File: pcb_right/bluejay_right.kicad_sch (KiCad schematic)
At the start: 60 parts, among them J2 SJ-43514, SW2B KEYSW, SW2C KEYSW, SW2D KEYSW, SW2E KEYSW, SW2F KEYSW, SW3A KEYSW, SW3B KEYSW, SW3C KEYSW, SW3D KEYSW, SW3E KEYSW, SW3F KEYSW, SW4A KEYSW, SW4B KEYSW, SW4C KEYSW, SW4D KEYSW, SW4E KEYSW, SW4F KEYSW, SW5A KEYSW, SW5B KEYSW, SW5C KEYSW, SW5D KEYSW, U2 MCP23017

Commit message: Some updates to schematics before moving to pcb design
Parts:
- C6: footprint (none) -> BlueJay footprints:CP_Radial_D4.0mm_P1.50mm
- C7: footprint (none) -> BlueJay footprints:C_Disc_D4.3mm_W1.9mm_P5.00mm
- J2: footprint CUI_SJ-43514 -> BlueJay footprints:CUI_SJ-43514
- R5, R6: footprint (none) -> BlueJay footprints:R_Axial_DIN0204_L3.6mm_D1.6mm_P5.08mm_Horizontal
- SWa1, SWa2, SWb1, SWc1, SWd1, SWe1: footprint (none) -> BlueJay footprints:Kailh_socket_MX
- SWa3: renamed from SW3A; footprint (none) -> BlueJay footprints:Kailh_socket_MX
- SWa4: renamed from SW4A; footprint (none) -> BlueJay footprints:Kailh_socket_MX
- SWa5: renamed from SW5A; footprint (none) -> BlueJay footprints:Kailh_socket_MX
- SWb2: renamed from SW2B; footprint (none) -> BlueJay footprints:Kailh_socket_MX
- SWb3: renamed from SW3B; footprint (none) -> BlueJay footprints:Kailh_socket_MX
- SWb4: renamed from SW4B; footprint (none) -> BlueJay footprints:Kailh_socket_MX
- SWb5: renamed from SW5B; footprint (none) -> BlueJay footprints:Kailh_socket_MX
- SWc2: renamed from SW2C; footprint (none) -> BlueJay footprints:Kailh_socket_MX
- SWc3: renamed from SW3C; footprint (none) -> BlueJay footprints:Kailh_socket_MX
- SWc4: renamed from SW4C; footprint (none) -> BlueJay footprints:Kailh_socket_MX
- SWc5: renamed from SW5C; footprint (none) -> BlueJay footprints:Kailh_socket_MX
- SWd2: renamed from SW2D; footprint (none) -> BlueJay footprints:Kailh_socket_MX
- SWd3: renamed from SW3D; footprint (none) -> BlueJay footprints:Kailh_socket_MX
- SWd4: renamed from SW4D; footprint (none) -> BlueJay footprints:Kailh_socket_MX
- SWd5: renamed from SW5D; footprint (none) -> BlueJay footprints:Kailh_socket_MX
- SWe2: renamed from SW2E; footprint (none) -> BlueJay footprints:Kailh_socket_MX
- SWe3: renamed from SW3E; footprint (none) -> BlueJay footprints:Kailh_socket_MX
- SWe4: renamed from SW4E; footprint (none) -> BlueJay footprints:Kailh_socket_MX
- SWf2: renamed from SW2F; footprint (none) -> BlueJay footprints:Kailh_socket_MX
- SWf3: renamed from SW3F; footprint (none) -> BlueJay footprints:Kailh_socket_MX
- SWf4: renamed from SW4F; footprint (none) -> BlueJay footprints:Kailh_socket_MX
- renumbered D3A to Da3, D4A to Da4, D5A to Da5, D2B to Db2, D3B to Db3, D4B to Db4, D5B to Db5, D2C to Dc2, D3C to Dc3, D4C to Dc4, D5C to Dc5, D2D to Dd2, D3D to Dd3, D4D to Dd4, D5D to Dd5, D2E to De2, D3E to De3, D4E to De4, D2F to Df2, D3F to Df3, D4F to Df4

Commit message: Work on PCBs
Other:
- title: (none) -> BlueJay Right
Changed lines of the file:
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@@
 (kicad_sch (version 20211123) (generator eeschema)
   (paper "USLetter")
+  (title_block
+    (title "BlueJay Right")
+  )
   (junction (at 194.31 62.23) (diameter 0) (color 0 0 0 0)
   )

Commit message: Begin work on right pcb
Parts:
- Da1, Da2, Da3, Da4, Da5, Db1, Db2, Db3, Db4, Db5, Dc1, Dc2, Dc3, Dc4, Dc5, Dd1, Dd2, Dd3, Dd4, Dd5, De1, De2, De3, De4, Df2, Df3, Df4: footprint Diode_THT_AKL:D_DO-35_SOD27_P7.62mm_Horizontal -> BlueJay footprints:D_DO-35_SOD27_P5.08mm_Horizontal
- SWa1, SWa2, SWa3, SWa4, SWa5, SWb1, SWb2, SWb3, SWb4, SWb5, SWc1, SWc2, SWc3, SWc4, SWc5, SWd1, SWd2, SWd3, SWd4, SWd5, SWe1, SWe2, SWe3, SWe4, SWf2, SWf3, SWf4: footprint BlueJay footprints:Kailh_socket_MX -> BlueJay footprints:SW_MX

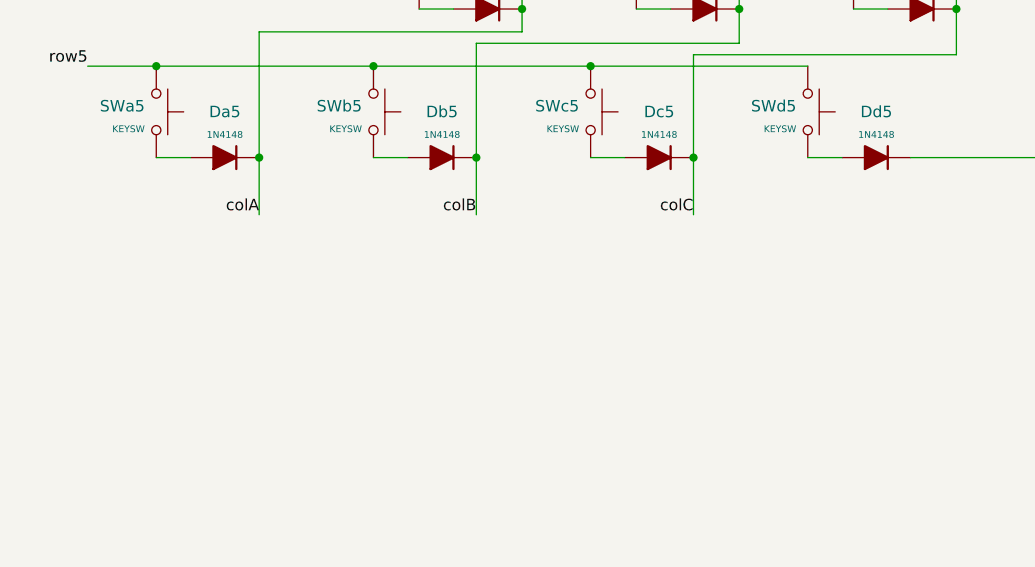
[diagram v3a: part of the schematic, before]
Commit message: Add mounting holes
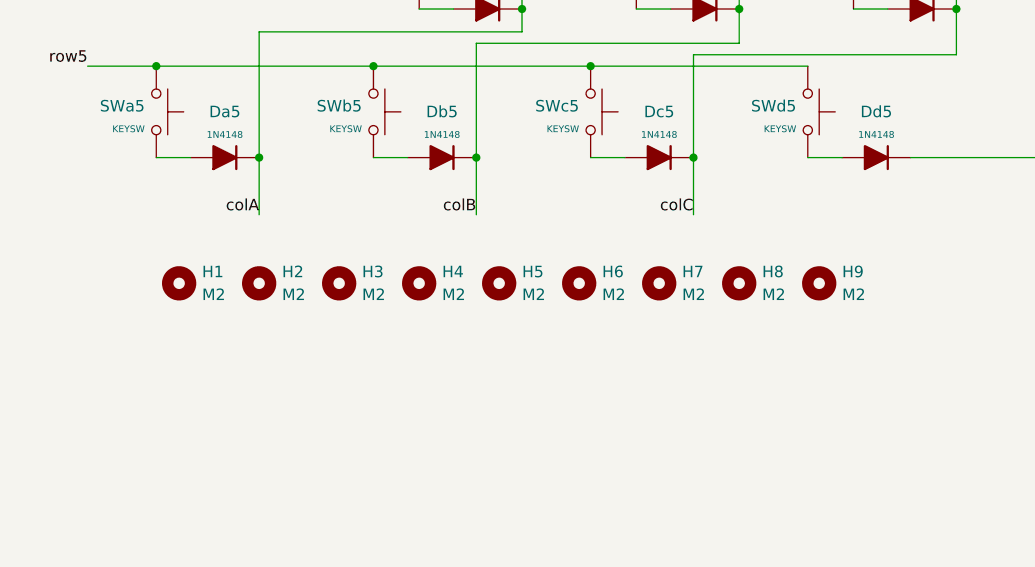
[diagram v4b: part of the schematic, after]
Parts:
- added H1, H2, H3, H4, H5, H6, H7, H8, H9: M2, MountingHole:MountingHole_2.2mm_M2_Pad, symbol Mechanical:MountingHole
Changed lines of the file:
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@@
     (pin "2")
+  )
+  (symbol (lib_id "Mechanical:MountingHole") (at 148.59 115.57 0) (unit 1)
+    (in_bom no) (on_board yes) (fields_autoplaced)
+    (property "Reference" "H7" (id 0) (at 151.13 114.2999 0)
+      (effects (font (size 1.27 1.27)) (justify left))
+    )
+    (property "Value" "M2" (id 1) (at 151.13 116.8399 0)
+      (effects (font (size 1.27 1.27)) (justify left))
+    )
+    (property "Footprint" "MountingHole:MountingHole_2.2mm_M2_Pad" (id 2) (at 148.59 115.57 0)
+      (effects (font (size 1.27 1.27)) hide)
+    )
+    (property "Datasheet" "~" (id 3) (at 148.59 115.57 0)
+      (effects (font (size 1.27 1.27)) hide)
+    )
   )
   (symbol (lib_id "BlueJaySymbolLibrary:Interface_Expansion_MCP23017_SP") (at 45.72 109.22 0) (unit 1)
@@
     (pin "9")
   )
+  (symbol (lib_id "Mechanical:MountingHole") (at 113.03 115.57 0) (unit 1)
+    (in_bom no) (on_board yes) (fields_autoplaced)
+    (property "Reference" "H3" (id 0) (at 115.57 114.2999 0)
+      (effects (font (size 1.27 1.27)) (justify left))
+    )
+    (property "Value" "M2" (id 1) (at 115.57 116.8399 0)
+      (effects (font (size 1.27 1.27)) (justify left))
+    )
+    (property "Footprint" "MountingHole:MountingHole_2.2mm_M2_Pad" (id 2) (at 113.03 115.57 0)
+      (effects (font (size 1.27 1.27)) hide)
+    )
+    (property "Datasheet" "~" (id 3) (at 113.03 115.57 0)
+      (effects (font (size 1.27 1.27)) hide)
+    )
+  )
   (symbol (lib_id "Diode_AKL:1N4148") (at 201.93 46.99 0) (mirror x) (unit 1)
     (in_bom yes) (on_board yes) (fields_autoplaced)
@@
     (pin "2")
   )
+  (symbol (lib_id "Mechanical:MountingHole") (at 104.14 115.57 0) (unit 1)
+    (in_bom no) (on_board yes) (fields_autoplaced)
+    (property "Reference" "H2" (id 0) (at 106.68 114.2999 0)
+      (effects (font (size 1.27 1.27)) (justify left))
+    )
+    (property "Value" "M2" (id 1) (at 106.68 116.8399 0)
+      (effects (font (size 1.27 1.27)) (justify left))
+    )
+    (property "Footprint" "MountingHole:MountingHole_2.2mm_M2_Pad" (id 2) (at 104.14 115.57 0)
+      (effects (font (size 1.27 1.27)) hide)
+    )
+    (property "Datasheet" "~" (id 3) (at 104.14 115.57 0)
+      (effects (font (size 1.27 1.27)) hide)
+    )
+  )
   (symbol (lib_id "power:GND") (at 45.72 139.7 0) (unit 1)
     (in_bom yes) (on_board yes) (fields_autoplaced)
@@
     )
     (pin "1")
+  )
+  (symbol (lib_id "Mechanical:MountingHole") (at 166.37 115.57 0) (unit 1)
+    (in_bom no) (on_board yes) (fields_autoplaced)
+    (property "Reference" "H9" (id 0) (at 168.91 114.2999 0)
+      (effects (font (size 1.27 1.27)) (justify left))
+    )
+    (property "Value" "M2" (id 1) (at 168.91 116.8399 0)
+      (effects (font (size 1.27 1.27)) (justify left))
+    )
+    (property "Footprint" "MountingHole:MountingHole_2.2mm_M2_Pad" (id 2) (at 166.37 115.57 0)
+      (effects (font (size 1.27 1.27)) hide)
+    )
+    (property "Datasheet" "~" (id 3) (at 166.37 115.57 0)
+      (effects (font (size 1.27 1.27)) hide)
+    )
   )
   (symbol (lib_id "BlueJaySymbolLibrary:Switch_SW_Push") (at 194.31 54.61 270) (mirror x) (unit 1)
@@
     (pin "2")
   )
+  (symbol (lib_id "Mechanical:MountingHole") (at 130.81 115.57 0) (unit 1)
+    (in_bom no) (on_board yes) (fields_autoplaced)
+    (property "Reference" "H5" (id 0) (at 133.35 114.2999 0)
+      (effects (font (size 1.27 1.27)) (justify left))
+    )
+    (property "Value" "M2" (id 1) (at 133.35 116.8399 0)
+      (effects (font (size 1.27 1.27)) (justify left))
+    )
+    (property "Footprint" "MountingHole:MountingHole_2.2mm_M2_Pad" (id 2) (at 130.81 115.57 0)
+      (effects (font (size 1.27 1.27)) hide)
+    )
+    (property "Datasheet" "~" (id 3) (at 130.81 115.57 0)
+      (effects (font (size 1.27 1.27)) hide)
+    )
+  )
   (symbol (lib_id "BlueJaySymbolLibrary:Device_R_Small") (at 55.88 46.99 0) (unit 1)
     (in_bom yes) (on_board yes) (fields_autoplaced)
@@
     (pin "1")
     (pin "2")
+  )
+  (symbol (lib_id "Mechanical:MountingHole") (at 139.7 115.57 0) (unit 1)
+    (in_bom no) (on_board yes) (fields_autoplaced)
+    (property "Reference" "H6" (id 0) (at 142.24 114.2999 0)
+      (effects (font (size 1.27 1.27)) (justify left))
+    )
+    (property "Value" "M2" (id 1) (at 142.24 116.8399 0)
+      (effects (font (size 1.27 1.27)) (justify left))
+    )
+    (property "Footprint" "MountingHole:MountingHole_2.2mm_M2_Pad" (id 2) (at 139.7 115.57 0)
+      (effects (font (size 1.27 1.27)) hide)
+    )
+    (property "Datasheet" "~" (id 3) (at 139.7 115.57 0)
+      (effects (font (size 1.27 1.27)) hide)
+    )
   )
   (symbol (lib_id "Diode_AKL:1N4148") (at 153.67 46.99 0) (mirror x) (unit 1)
@@
     (pin "1")
   )
+  (symbol (lib_id "Mechanical:MountingHole") (at 121.92 115.57 0) (unit 1)
+    (in_bom no) (on_board yes) (fields_autoplaced)
+    (property "Reference" "H4" (id 0) (at 124.46 114.2999 0)
+      (effects (font (size 1.27 1.27)) (justify left))
+    )
+    (property "Value" "M2" (id 1) (at 124.46 116.8399 0)
+      (effects (font (size 1.27 1.27)) (justify left))
+    )
+    (property "Footprint" "MountingHole:MountingHole_2.2mm_M2_Pad" (id 2) (at 121.92 115.57 0)
+      (effects (font (size 1.27 1.27)) hide)
+    )
+    (property "Datasheet" "~" (id 3) (at 121.92 115.57 0)
+      (effects (font (size 1.27 1.27)) hide)
+    )
+  )
   (symbol (lib_id "BlueJaySymbolLibrary:Switch_SW_Push") (at 121.92 67.31 270) (mirror x) (unit 1)
     (in_bom yes) (on_board yes) (fields_autoplaced)
@@
     (pin "1")
     (pin "2")
+  )
+  (symbol (lib_id "Mechanical:MountingHole") (at 95.25 115.57 0) (unit 1)
+    (in_bom no) (on_board yes) (fields_autoplaced)
+    (property "Reference" "H1" (id 0) (at 97.79 114.2999 0)
+      (effects (font (size 1.27 1.27)) (justify left))
+    )
+    (property "Value" "M2" (id 1) (at 97.79 116.8399 0)
+      (effects (font (size 1.27 1.27)) (justify left))
+    )
+    (property "Footprint" "MountingHole:MountingHole_2.2mm_M2_Pad" (id 2) (at 95.25 115.57 0)
+      (effects (font (size 1.27 1.27)) hide)
+    )
+    (property "Datasheet" "~" (id 3) (at 95.25 115.57 0)
+      (effects (font (size 1.27 1.27)) hide)
+    )
   )
   (symbol (lib_id "BlueJaySymbolLibrary:Switch_SW_Push") (at 146.05 80.01 270) (mirror x) (unit 1)
@@
     (pin "1")
   )
+  (symbol (lib_id "Mechanical:MountingHole") (at 157.48 115.57 0) (unit 1)
+    (in_bom no) (on_board yes) (fields_autoplaced)
+    (property "Reference" "H8" (id 0) (at 160.02 114.2999 0)
+      (effects (font (size 1.27 1.27)) (justify left))
+    )
+    (property "Value" "M2" (id 1) (at 160.02 116.8399 0)
+      (effects (font (size 1.27 1.27)) (justify left))
+    )
+    (property "Footprint" "MountingHole:MountingHole_2.2mm_M2_Pad" (id 2) (at 157.48 115.57 0)
+      (effects (font (size 1.27 1.27)) hide)
+    )
+    (property "Datasheet" "~" (id 3) (at 157.48 115.57 0)
+      (effects (font (size 1.27 1.27)) hide)
+    )
+  )
   (symbol (lib_id "Diode_AKL:1N4148") (at 153.67 72.39 0) (mirror x) (unit 1)
     (in_bom yes) (on_board yes) (fields_autoplaced)
@@
       (reference "Df4") (unit 1) (value "1N4148") (footprint "BlueJay footprints:D_DO-35_SOD27_P5.08mm_Horizontal")
     )
+    (path "/e3a864c6-2e05-4a63-b022-da7d340645e3"
+      (reference "H1") (unit 1) (value "M2") (footprint "MountingHole:MountingHole_2.2mm_M2_Pad")
+    )
+    (path "/29cea050-3e29-419d-ad47-3e79a1eb9101"
+      (reference "H2") (unit 1) (value "M2") (footprint "MountingHole:MountingHole_2.2mm_M2_Pad")
+    )
+    (path "/17614258-4f06-4822-913f-021afed04082"
+      (reference "H3") (unit 1) (value "M2") (footprint "MountingHole:MountingHole_2.2mm_M2_Pad")
+    )
+    (path "/e175d568-d75e-4a79-8707-a3c7001d62d8"
+      (reference "H4") (unit 1) (value "M2") (footprint "MountingHole:MountingHole_2.2mm_M2_Pad")
+    )
+    (path "/6076ed14-f492-4b0a-917b-dfd270a3bad8"
+      (reference "H5") (unit 1) (value "M2") (footprint "MountingHole:MountingHole_2.2mm_M2_Pad")
+    )
+    (path "/898f562a-635b-4ca8-9b29-632b29153076"
+      (reference "H6") (unit 1) (value "M2") (footprint "MountingHole:MountingHole_2.2mm_M2_Pad")
+    )
+    (path "/122e03f9-b490-4614-ab57-8a45c16d7cab"
+      (reference "H7") (unit 1) (value "M2") (footprint "MountingHole:MountingHole_2.2mm_M2_Pad")
+    )
+    (path "/ef6bf8a6-53c5-40a0-b55f-f0f6022fe6b3"
+      (reference "H8") (unit 1) (value "M2") (footprint "MountingHole:MountingHole_2.2mm_M2_Pad")
+    )
+    (path "/2f72a678-d445-4b98-b401-be2796bd34c3"
+      (reference "H9") (unit 1) (value "M2") (footprint "MountingHole:MountingHole_2.2mm_M2_Pad")
+    )
     (path "/36a90cbb-ec70-4202-aacd-9cf629bac560"

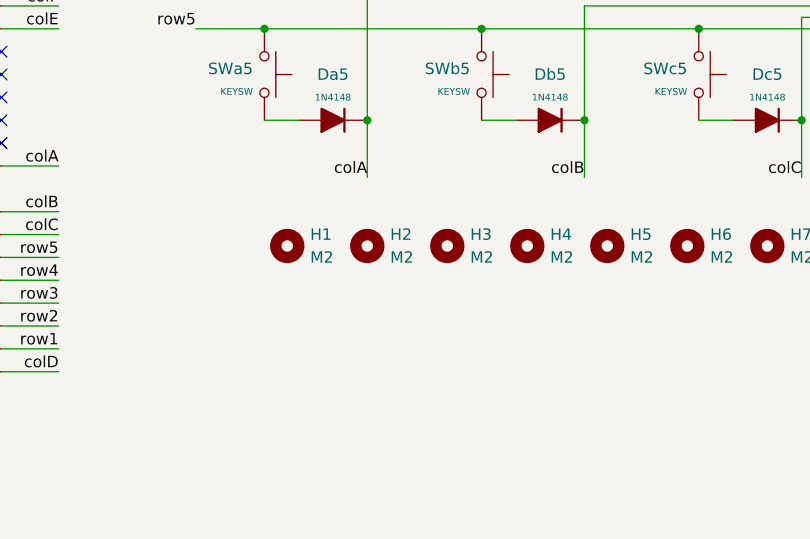
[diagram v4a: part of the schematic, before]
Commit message: Ground a couple mounting holes so as to ground plate and base too
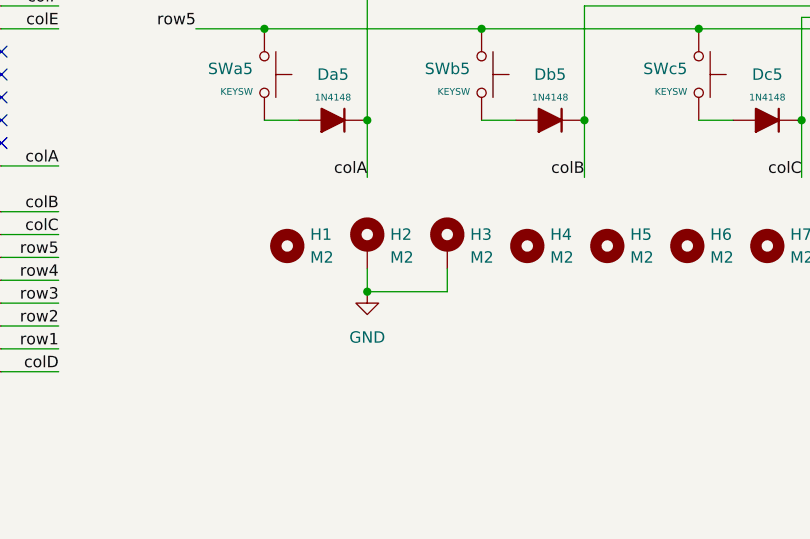
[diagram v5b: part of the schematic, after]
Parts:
- H2, H3: symbol Mechanical:MountingHole -> Mechanical:MountingHole_Pad; now in the parts list
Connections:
- net GND: now also H2.1, H3.1
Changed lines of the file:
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@@
   (junction (at 170.18 49.53) (diameter 0) (color 0 0 0 0)
+  )
+  (junction (at 104.14 120.65) (diameter 0) (color 0 0 0 0)
   )
   (no_connect (at 63.5 101.6))
@@
     (stroke (width 0) (type default) (color 0 0 0 0))
   )
+  (wire (pts (xy 113.03 118.11) (xy 113.03 120.65))
+    (stroke (width 0) (type default) (color 0 0 0 0))
+  )
   (wire (pts (xy 152.4 90.17) (xy 152.4 101.6))
     (stroke (width 0) (type default) (color 0 0 0 0))
@@
     (stroke (width 0) (type default) (color 0 0 0 0))
   )
+  (wire (pts (xy 113.03 120.65) (xy 104.14 120.65))
+    (stroke (width 0) (type default) (color 0 0 0 0))
+  )
   (wire (pts (xy 133.35 46.99) (xy 133.35 59.69))
     (stroke (width 0) (type default) (color 0 0 0 0))
@@
   )
   (wire (pts (xy 222.25 46.99) (xy 218.44 46.99))
+    (stroke (width 0) (type default) (color 0 0 0 0))
+  )
+  (wire (pts (xy 104.14 118.11) (xy 104.14 120.65))
     (stroke (width 0) (type default) (color 0 0 0 0))
   )
@@
     (pin "9")
   )
-  (symbol (lib_id "Mechanical:MountingHole") (at 113.03 115.57 0) (unit 1)
-    (in_bom no) (on_board yes) (fields_autoplaced)
+  (symbol (lib_id "Mechanical:MountingHole_Pad") (at 113.03 115.57 0) (unit 1)
+    (in_bom yes) (on_board yes) (fields_autoplaced)
     (property "Reference" "H3" (id 0) (at 115.57 114.2999 0)
       (effects (font (size 1.27 1.27)) (justify left))
@@
       (effects (font (size 1.27 1.27)) hide)
     )
+    (pin "1")
   )
   (symbol (lib_id "Diode_AKL:1N4148") (at 201.93 46.99 0) (mirror x) (unit 1)
@@
     (pin "2")
   )
-  (symbol (lib_id "Mechanical:MountingHole") (at 104.14 115.57 0) (unit 1)
-    (in_bom no) (on_board yes) (fields_autoplaced)
+  (symbol (lib_id "Mechanical:MountingHole_Pad") (at 104.14 115.57 0) (unit 1)
+    (in_bom yes) (on_board yes) (fields_autoplaced)
     (property "Reference" "H2" (id 0) (at 106.68 114.2999 0)
       (effects (font (size 1.27 1.27)) (justify left))
@@
       (effects (font (size 1.27 1.27)) hide)
     )
+    (pin "1")
   )
   (symbol (lib_id "power:GND") (at 45.72 139.7 0) (unit 1)
@@
     (pin "2")
   )
+  (symbol (lib_id "power:GND") (at 104.14 120.65 0) (unit 1)
+    (in_bom yes) (on_board yes) (fields_autoplaced)
+    (property "Reference" "#PWR0110" (id 0) (at 104.14 127 0)
+      (effects (font (size 1.27 1.27)) hide)
+    )
+    (property "Value" "GND" (id 1) (at 104.14 125.73 0))
+    (property "Footprint" "" (id 2) (at 104.14 120.65 0)
+      (effects (font (size 1.27 1.27)) hide)
+    )
+    (property "Datasheet" "" (id 3) (at 104.14 120.65 0)
+      (effects (font (size 1.27 1.27)) hide)
+    )
+    (pin "1")
+  )
   (symbol (lib_id "power:GND") (at 41.91 62.23 0) (unit 1)
     (in_bom yes) (on_board yes) (fields_autoplaced)
@@
       (reference "#PWR0109") (unit 1) (value "VCC") (footprint "")
     )
+    (path "/5c628fb1-db6b-4a2b-bba3-1f81260cfadb"
+      (reference "#PWR0110") (unit 1) (value "GND") (footprint "")
+    )
     (path "/248864a2-91ef-4d14-87e7-7b68a9c3eb73"
